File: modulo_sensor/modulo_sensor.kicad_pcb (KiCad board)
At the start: 2 copper layers, 90 x 27 mm, 33 parts, among them J1 Conn_01x08_Pin, U1 74HC14DR2G

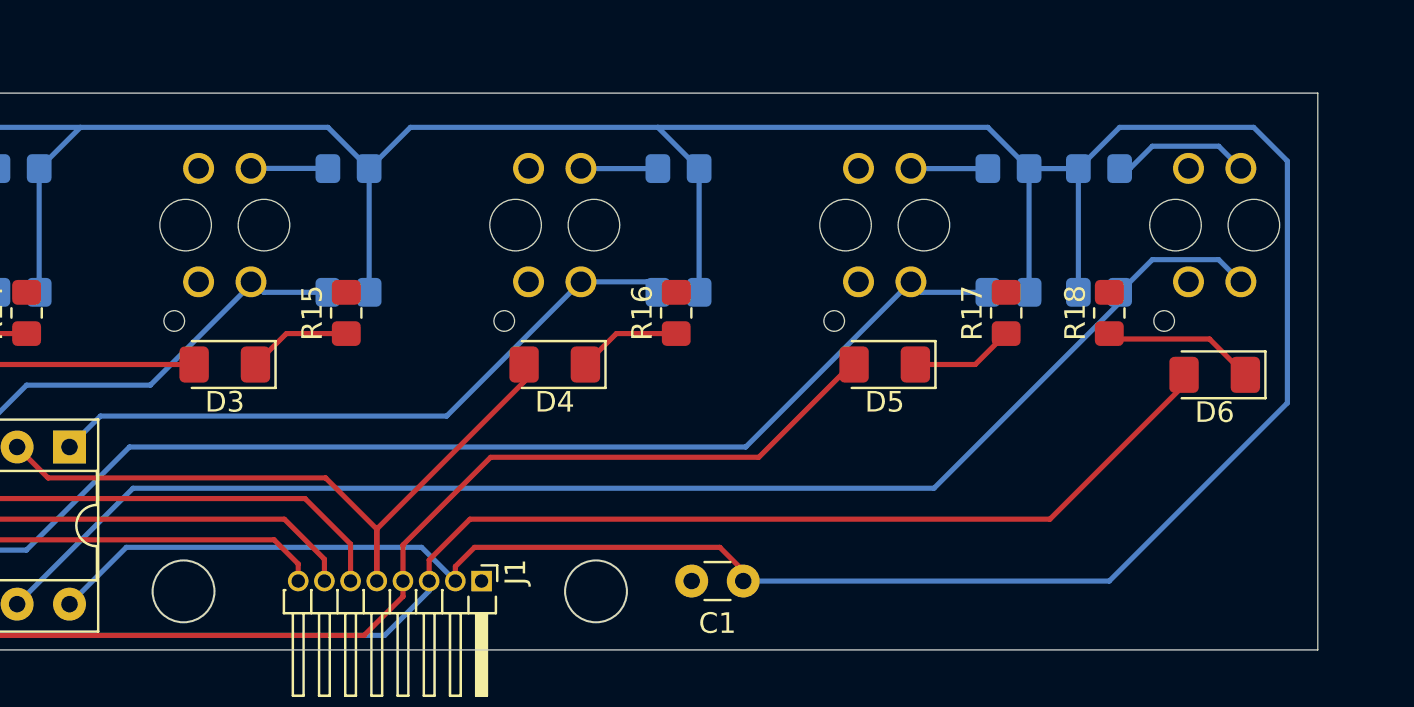
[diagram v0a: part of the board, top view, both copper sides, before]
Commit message: refactor: Cambio de margen de rutas a 0,3mm y arreglo algunos checks
Las infracciones son por la cercania de los pines del conector J1
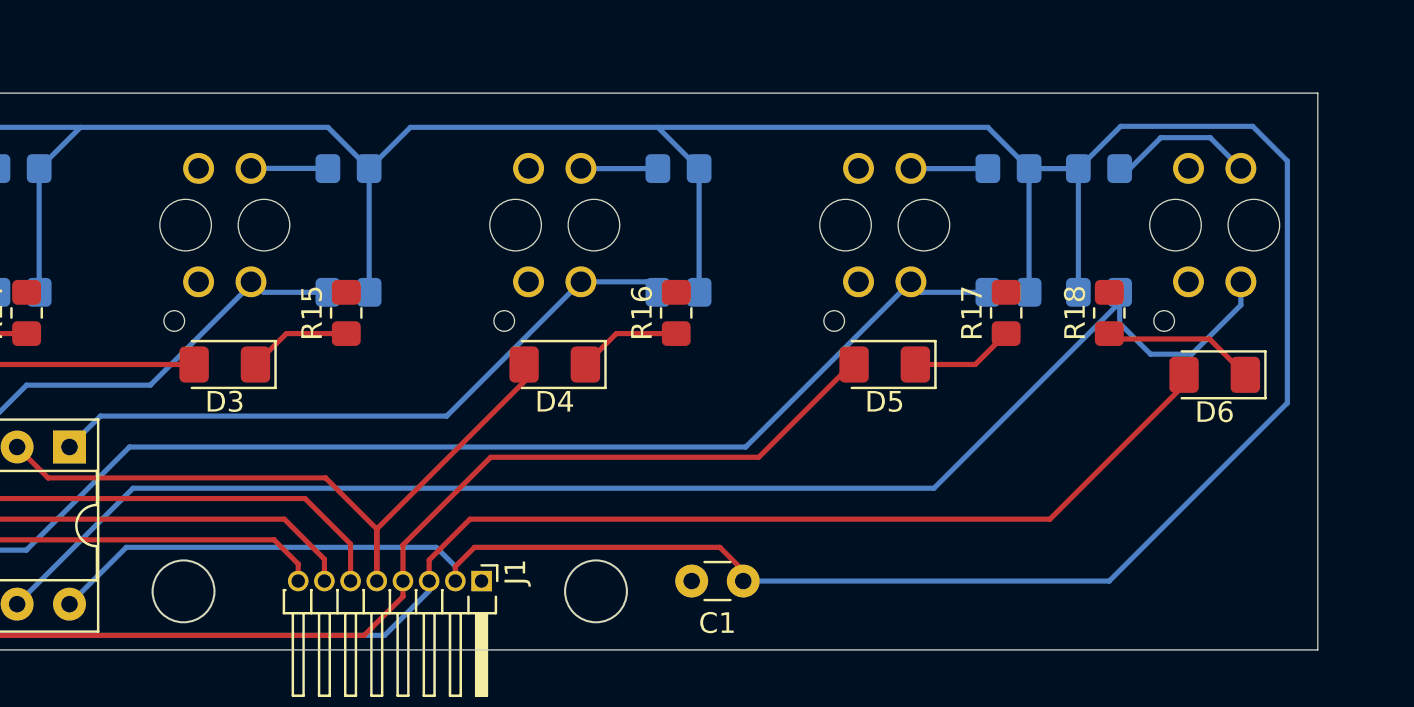
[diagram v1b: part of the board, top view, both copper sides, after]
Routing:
- net /Sensor6: track 67.0 -> 70.1 mm
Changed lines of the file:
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@@
 	)
 	(setup
+		(stackup
+			(layer "F.SilkS"
+				(type "Top Silk Screen")
+			)
+			(layer "F.Paste"
+				(type "Top Solder Paste")
+			)
+			(layer "F.Mask"
+				(type "Top Solder Mask")
+				(thickness 0.01)
+			)
+			(layer "F.Cu"
+				(type "copper")
+				(thickness 0.035)
+			)
+			(layer "dielectric 1"
+				(type "core")
+				(thickness 1.51)
+				(material "FR4")
+				(epsilon_r 4.5)
+				(loss_tangent 0.02)
+			)
+			(layer "B.Cu"
+				(type "copper")
+				(thickness 0.035)
+			)
+			(layer "B.Mask"
+				(type "Bottom Solder Mask")
+				(thickness 0.01)
+			)
+			(layer "B.Paste"
+				(type "Bottom Solder Paste")
+			)
+			(layer "B.SilkS"
+				(type "Bottom Silk Screen")
+			)
+			(copper_finish "None")
+			(dielectric_constraints no)
+		)
 		(pad_to_mask_clearance 0)
 		(allow_soldermask_bridges_in_footprints no)
@@
 	)
 	(segment
-		(start 85.834729 78.365271)
-		(end 100.155254 78.365271)
+		(start 81.609983 66)
+		(end 81.609983 60)
 		(width 0.25)
 		(layer "B.Cu")
@@
 	)
 	(segment
-		(start 81.609983 66)
-		(end 81.609983 60)
+		(start 97.609983 60)
+		(end 99.609983 58)
 		(width 0.25)
 		(layer "B.Cu")
@@
 	)
 	(segment
-		(start 97.609983 60)
-		(end 99.609983 58)
+		(start 83.08 81.12)
+		(end 85.834729 78.365271)
 		(width 0.25)
 		(layer "B.Cu")
@@
 	)
 	(segment
+		(start 115.75 80)
+		(end 133.5 80)
+		(width 0.25)
+		(layer "B.Cu")
+		(net 1)
+	)
+	(segment
 		(start 129.609983 60)
 		(end 132 60)
@@
 	)
 	(segment
-		(start 115.75 80)
-		(end 133.5 80)
+		(start 85.834729 78.365271)
+		(end 100.865271 78.365271)
 		(width 0.25)
 		(layer "B.Cu")
@@
 	)
 	(segment
-		(start 140.5 58)
-		(end 134 58)
+		(start 133.5 80)
+		(end 142.134983 71.365017)
 		(width 0.25)
 		(layer "B.Cu")
@@
 	)
 	(segment
-		(start 142.134983 71.365017)
-		(end 142.134983 59.634983)
+		(start 113.609983 66)
+		(end 113.609983 60)
 		(width 0.25)
 		(layer "B.Cu")
@@
 	)
 	(segment
-		(start 83.08 81.12)
-		(end 85.834729 78.365271)
+		(start 101.789983 79.289983)
+		(end 101.789983 80)
 		(width 0.25)
 		(layer "B.Cu")
@@
 	)
 	(segment
-		(start 142.134983 59.634983)
-		(end 140.5 58)
+		(start 134.05 57.95)
+		(end 132 60)
 		(width 0.25)
 		(layer "B.Cu")
@@
 	)
 	(segment
-		(start 113.609983 66)
-		(end 113.609983 60)
+		(start 65 66)
+		(end 65 60)
 		(width 0.25)
 		(layer "B.Cu")
@@
 	)
 	(segment
-		(start 100.155254 78.365271)
-		(end 101.789983 80)
+		(start 83.609983 58)
+		(end 67 58)
 		(width 0.25)
 		(layer "B.Cu")
@@
 	)
 	(segment
-		(start 133.5 80)
-		(end 142.134983 71.365017)
+		(start 142.134983 59.634983)
+		(end 140.45 57.95)
 		(width 0.25)
 		(layer "B.Cu")
@@
 	)
 	(segment
-		(start 134 58)
-		(end 132 60)
+		(start 140.45 57.95)
+		(end 134.05 57.95)
 		(width 0.25)
 		(layer "B.Cu")
@@
 	)
 	(segment
-		(start 65 66)
-		(end 65 60)
+		(start 111.609983 58)
+		(end 113.609983 60)
 		(width 0.25)
 		(layer "B.Cu")
@@
 	)
 	(segment
-		(start 83.609983 58)
-		(end 67 58)
+		(start 111.609983 58)
+		(end 127.609983 58)
 		(width 0.25)
 		(layer "B.Cu")
@@
 	)
 	(segment
-		(start 111.609983 58)
-		(end 113.609983 60)
+		(start 142.134983 71.365017)
+		(end 142.134983 59.634983)
 		(width 0.25)
 		(layer "B.Cu")
@@
 	)
 	(segment
-		(start 111.609983 58)
-		(end 127.609983 58)
+		(start 100.865271 78.365271)
+		(end 101.789983 79.289983)
 		(width 0.25)
 		(layer "B.Cu")
@@
 	)
 	(segment
-		(start 134.5 60)
-		(end 135.585 58.915)
+		(start 138.389983 58.5)
+		(end 139.879983 59.99)
 		(width 0.25)
 		(layer "B.Cu")
@@
 	)
 	(segment
-		(start 135.585 58.915)
-		(end 138.804983 58.915)
+		(start 136 58.5)
+		(end 138.389983 58.5)
 		(width 0.25)
 		(layer "B.Cu")
@@
 	)
 	(segment
-		(start 138.804983 58.915)
-		(end 139.879983 59.99)
+		(start 134 60)
+		(end 134.5 60)
 		(width 0.25)
 		(layer "B.Cu")
@@
 	)
 	(segment
-		(start 134 60)
-		(end 134.5 60)
+		(start 134.5 60)
+		(end 136 58.5)
 		(width 0.25)
 		(layer "B.Cu")
@@
 	)
 	(segment
-		(start 135.585 64.415)
-		(end 138.804983 64.415)
+		(start 134 66)
+		(end 134 66.5)
 		(width 0.25)
 		(layer "B.Cu")
@@
 	)
 	(segment
-		(start 138.804983 64.415)
-		(end 139.879983 65.49)
+		(start 86.16 75.5)
+		(end 80.54 81.12)
 		(width 0.25)
 		(layer "B.Cu")
@@
 	)
 	(segment
-		(start 134 66)
-		(end 134 66.5)
+		(start 135.5 69)
+		(end 137.5 69)
 		(width 0.25)
 		(layer "B.Cu")
@@
 	)
 	(segment
-		(start 86.16 75.5)
-		(end 80.54 81.12)
+		(start 134 67.5)
+		(end 135.5 69)
 		(width 0.25)
 		(layer "B.Cu")
@@
 	)
 	(segment
-		(start 134 66)
-		(end 135.585 64.415)
+		(start 137.5 69)
+		(end 139.879983 66.620017)
 		(width 0.25)
 		(layer "B.Cu")
@@
 		(width 0.25)
 		(layer "B.Cu")
+		(net 26)
+	)
+	(segment
+		(start 139.879983 66.620017)
+		(end 139.879983 65.49)
+		(width 0.25)
+		(layer "B.Cu")
+		(net 26)
+	)
+	(segment
+		(start 134 66)
+		(end 134 67.5)
+		(width 0.25)
+		(layer "B.Cu")

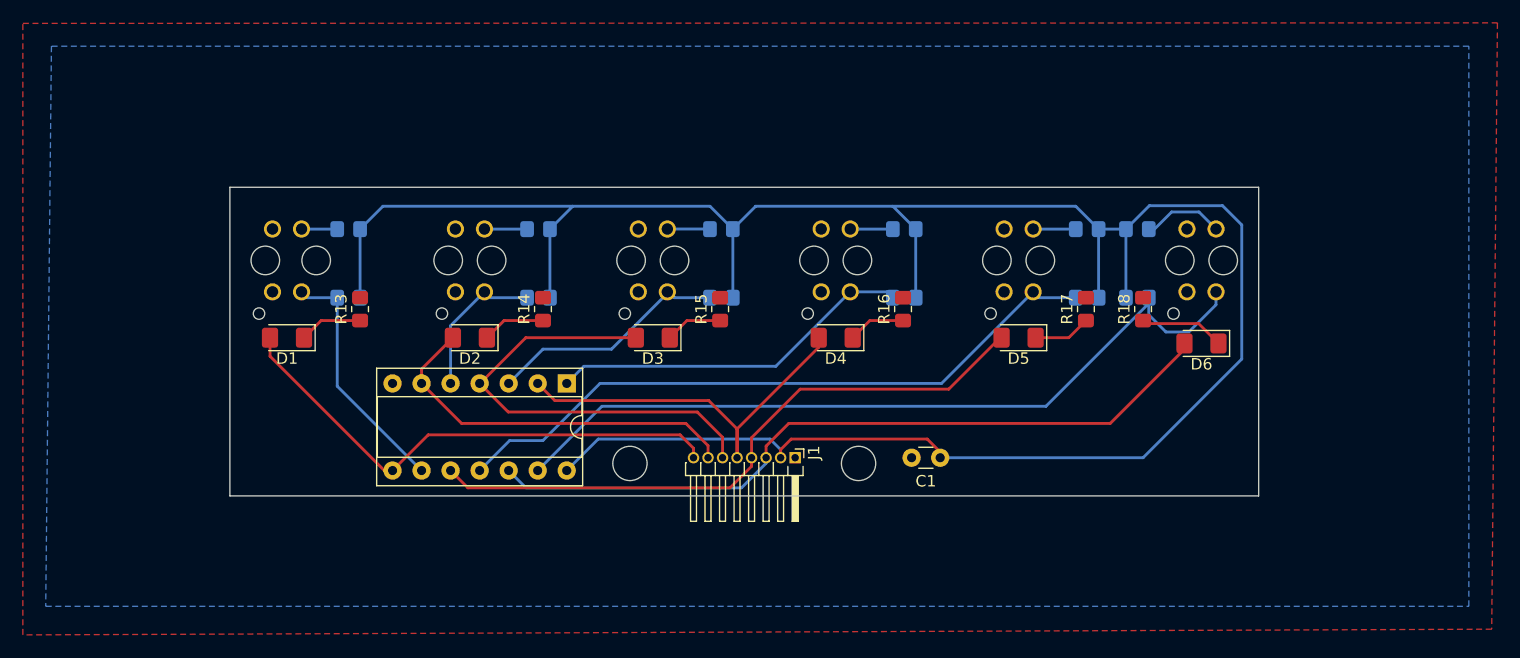
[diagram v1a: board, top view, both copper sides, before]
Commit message: refactor: Actualizo el ancho de las pistas a 0,6
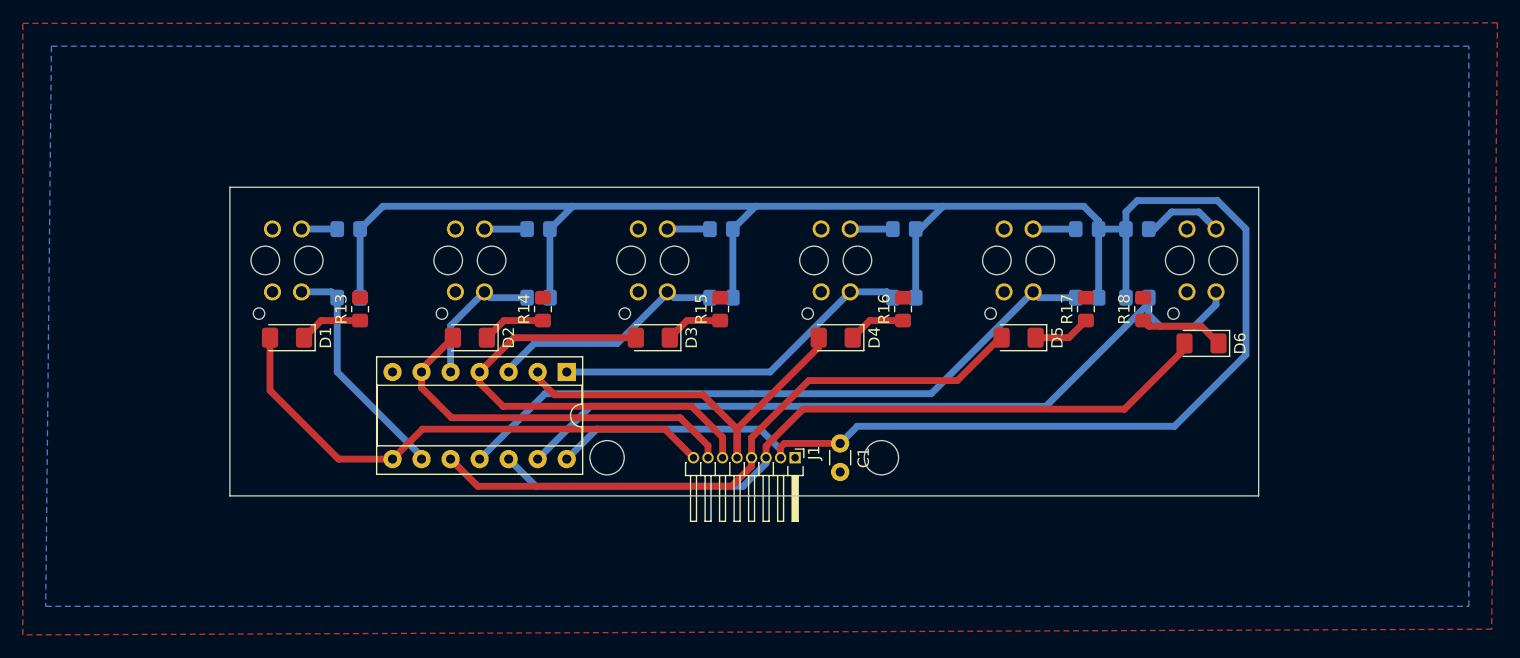
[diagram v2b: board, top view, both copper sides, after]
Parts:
- moved C1 8.84 mm to (107.0, 78.8), turned to -90 degrees
- moved U1 1.00 mm to (83.1, 72.5)
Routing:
- net vcc: track 202.5 -> 204.6 mm
- net /Sensor2: track 13.2 -> 12.2 mm
- net /Sensor1: track 21.5 -> 20.5 mm
- net /Led_Sensor1: track 45.5 -> 46.5 mm
- net /Sensor6: track 70.1 -> 69.3 mm
- net /Led_Sensor4: track 34.5 -> 35.3 mm
- net /Led_Sensor3: track 40.3 -> 40.8 mm
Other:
- outline, holes or cut-outs redrawn
- board text removed: "Anterior medida"

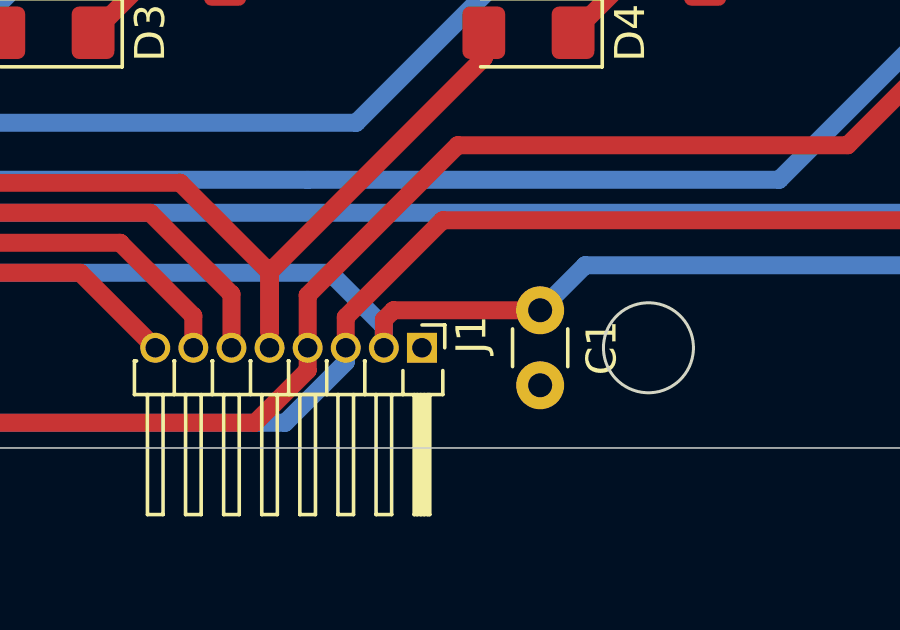
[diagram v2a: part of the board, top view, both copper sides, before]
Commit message: fix: Agrego valor a la huella del capacitor
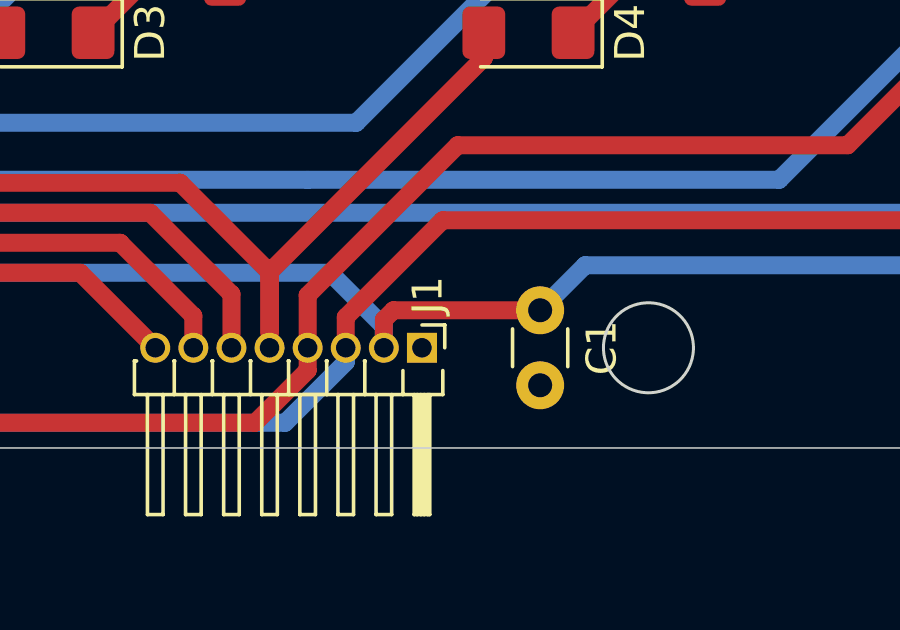
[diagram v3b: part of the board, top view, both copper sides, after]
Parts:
- C1: value C -> 10u1
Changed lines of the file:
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@@
 		(tags "Through hole angled pin header THT 1x08 1.27mm single row")
 		(property "Reference" "J1"
-			(at -0.435 -1.65 90)
+			(at -1.75 -0.190017 90)
 			(layer "F.SilkS")
 			(effects
@@
 		)
 		(property "Value" "Conn_01x08_Pin"
-			(at -2.795 4.47 0)
+			(at -3.5 4.47 0)
 			(layer "F.Fab")
 			(effects
@@
 			)
 		)
-		(property "Value" "C"
+		(property "Value" "10u1"
 			(at 1.25 2.05 90)
 			(layer "F.Fab")

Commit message: refactor: Alejo pistas de los bordes (por las dudas)
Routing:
- net /Sensor6: track 69.3 -> 74.1 mm
- net /Sensor4: track 31.6 -> 33.3 mm
- net /Sensor5: track 58.4 -> 59.8 mm
- net /Sensor3: track 20.9 -> 21.5 mm
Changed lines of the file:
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@@
 		(at 90.609983 62.74 90)
 		(property "Reference" "Sensor3"
-			(at -1.76355 4.57476 90)
+			(at -6.5 0 0)
 			(layer "B.SilkS")
 			(effects
@@
 		(at 74.609983 62.74 90)
 		(property "Reference" "Sensor2"
-			(at -1.76355 4.57476 90)
+			(at -6.5 0 0)
 			(layer "B.SilkS")
 			(effects
@@
 		(at 138.609983 62.74 90)
 		(property "Reference" "Sensor6"
-			(at -1.76355 3.84 90)
+			(at -6.5 0 0)
 			(layer "B.SilkS")
 			(effects
@@
 		(at 122.609983 62.74 90)
 		(property "Reference" "Sensor5"
-			(at -1.76355 4.57476 90)
+			(at -6.5 0 0)
 			(layer "B.SilkS")
 			(effects
@@
 		(at 58.609983 62.74 90)
 		(property "Reference" "Sensor1"
-			(at -1.76355 4.57476 -90)
+			(at -6.5 0 0)
 			(layer "B.SilkS")
 			(effects
@@
 		(model "${KIPRJMOD}/step/TCRT5000.step"
 			(offset
-				(xyz -1 0.25 0)
+				(xyz -1 -0 0)
 			)
 			(scale
@@
 		(at 106.609983 62.74 90)
 		(property "Reference" "Sensor4"
-			(at -1.76355 4.57476 90)
+			(at -6.5 0 0)
 			(layer "B.SilkS")
 			(effects
@@
 	)
 	(segment
+		(start 75.879983 67.620017)
+		(end 75.879983 65.49)
+		(width 0.6)
+		(layer "B.Cu")
+		(net 18)
+	)
+	(segment
 		(start 79.609983 66)
 		(end 76.389983 66)
@@
 	)
 	(segment
-		(start 72.92 68.449983)
-		(end 75.879983 65.49)
+		(start 72.92 72.5)
+		(end 72.92 70.58)
 		(width 0.6)
 		(layer "B.Cu")
@@
 	)
 	(segment
-		(start 76.389983 66)
-		(end 75.879983 65.49)
+		(start 72.92 70.58)
+		(end 75.879983 67.620017)
 		(width 0.6)
 		(layer "B.Cu")
@@
 	)
 	(segment
-		(start 72.92 72.5)
-		(end 72.92 68.449983)
+		(start 76.389983 66)
+		(end 75.879983 65.49)
 		(width 0.6)
 		(layer "B.Cu")
@@
 	)
 	(segment
-		(start 80.25 70)
-		(end 87.5 70)
+		(start 91.99 65.49)
+		(end 92.5 66)
 		(width 0.6)
 		(layer "B.Cu")
@@
 	)
 	(segment
-		(start 91.99 65.49)
-		(end 92.5 66)
+		(start 78 72.5)
+		(end 78 72.25)
 		(width 0.6)
 		(layer "B.Cu")
@@
 	)
 	(segment
-		(start 78 72.5)
-		(end 78 72.25)
+		(start 80.25 70)
+		(end 88.5 70)
 		(width 0.6)
 		(layer "B.Cu")
@@
 	)
 	(segment
-		(start 91.879983 65.49)
-		(end 91.99 65.49)
+		(start 91.879983 66.620017)
+		(end 91.879983 65.49)
 		(width 0.6)
 		(layer "B.Cu")
@@
 	)
 	(segment
-		(start 87.5 70)
-		(end 91.879983 65.620017)
+		(start 88.5 70)
+		(end 91.879983 66.620017)
 		(width 0.6)
 		(layer "B.Cu")
@@
 	)
 	(segment
-		(start 91.879983 65.620017)
-		(end 91.879983 65.49)
+		(start 91.879983 65.49)
+		(end 91.99 65.49)
 		(width 0.6)
 		(layer "B.Cu")
@@
 	)
 	(segment
-		(start 107.879983 65.49)
-		(end 111.099983 65.49)
+		(start 107.879983 68.370017)
+		(end 107.879983 65.49)
 		(width 0.6)
 		(layer "B.Cu")
@@
 	)
 	(segment
-		(start 100.869983 72.5)
-		(end 107.879983 65.49)
+		(start 83.08 72.5)
+		(end 103.75 72.5)
 		(width 0.6)
 		(layer "B.Cu")
@@
 	)
 	(segment
-		(start 83.08 72.5)
-		(end 100.869983 72.5)
+		(start 107.879983 65.49)
+		(end 111.099983 65.49)
+		(width 0.6)
+		(layer "B.Cu")
+		(net 22)
+	)
+	(segment
+		(start 103.75 72.5)
+		(end 107.879983 68.370017)
 		(width 0.6)
 		(layer "B.Cu")
@@
 	)
 	(segment
-		(start 99.25 74.4)
-		(end 114.969983 74.4)
+		(start 81.18 74.4)
+		(end 117.35 74.4)
 		(width 0.6)
 		(layer "B.Cu")
@@
 	)
 	(segment
-		(start 127.609983 66)
-		(end 124.389983 66)
+		(start 117.35 74.4)
+		(end 123.879983 67.870017)
 		(width 0.6)
 		(layer "B.Cu")
@@
 	)
 	(segment
-		(start 75.46 80.12)
-		(end 81.18 74.4)
+		(start 123.879983 67.870017)
+		(end 123.879983 65.49)
 		(width 0.6)
 		(layer "B.Cu")
@@
 	)
 	(segment
-		(start 114.969983 74.4)
-		(end 123.879983 65.49)
+		(start 127.609983 66)
+		(end 124.389983 66)
 		(width 0.6)
 		(layer "B.Cu")
@@
 	)
 	(segment
-		(start 81.18 74.4)
-		(end 99.25 74.4)
+		(start 75.46 80.12)
+		(end 81.18 74.4)
 		(width 0.6)
 		(layer "B.Cu")
@@
 	)
 	(segment
-		(start 138 68.5)
-		(end 139.879983 66.620017)
-		(width 0.6)
-		(layer "B.Cu")
-		(net 26)
-	)
-	(segment
-		(start 139.879983 66.620017)
-		(end 139.879983 65.49)
+		(start 132 75.5)
+		(end 139.879983 67.620017)
 		(width 0.6)
 		(layer "B.Cu")
@@
 	)
 	(segment
-		(start 134 66)
-		(end 134 67.5)
+		(start 80.54 80.12)
+		(end 85.16 75.5)
 		(width 0.6)
 		(layer "B.Cu")
@@
 	(segment
 		(start 134 66)
-		(end 134 66.5)
-		(width 0.6)
-		(layer "B.Cu")
-		(net 26)
-	)
-	(segment
-		(start 134 66.5)
-		(end 125 75.5)
-		(width 0.6)
-		(layer "B.Cu")
-		(net 26)
-	)
-	(segment
-		(start 135 68.5)
-		(end 138 68.5)
-		(width 0.6)
-		(layer "B.Cu")
-		(net 26)
-	)
-	(segment
-		(start 134 67.5)
-		(end 135 68.5)
+		(end 134 73.5)
 		(width 0.6)
 		(layer "B.Cu")
@@
 	)
 	(segment
-		(start 125 75.5)
-		(end 85.16 75.5)
+		(start 85.16 75.5)
+		(end 132 75.5)
 		(width 0.6)
 		(layer "B.Cu")
@@
 	)
 	(segment
-		(start 85.16 75.5)
-		(end 80.54 80.12)
+		(start 139.879983 67.620017)
+		(end 139.879983 65.49)
 		(width 0.6)
 		(layer "B.Cu")
